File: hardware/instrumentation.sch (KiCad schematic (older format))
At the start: 27 parts, among them U2 TMP235, U3 TMP235, U4 TMP235, U5 TMUX1309, U6 TMUX1309, U7 LMV554

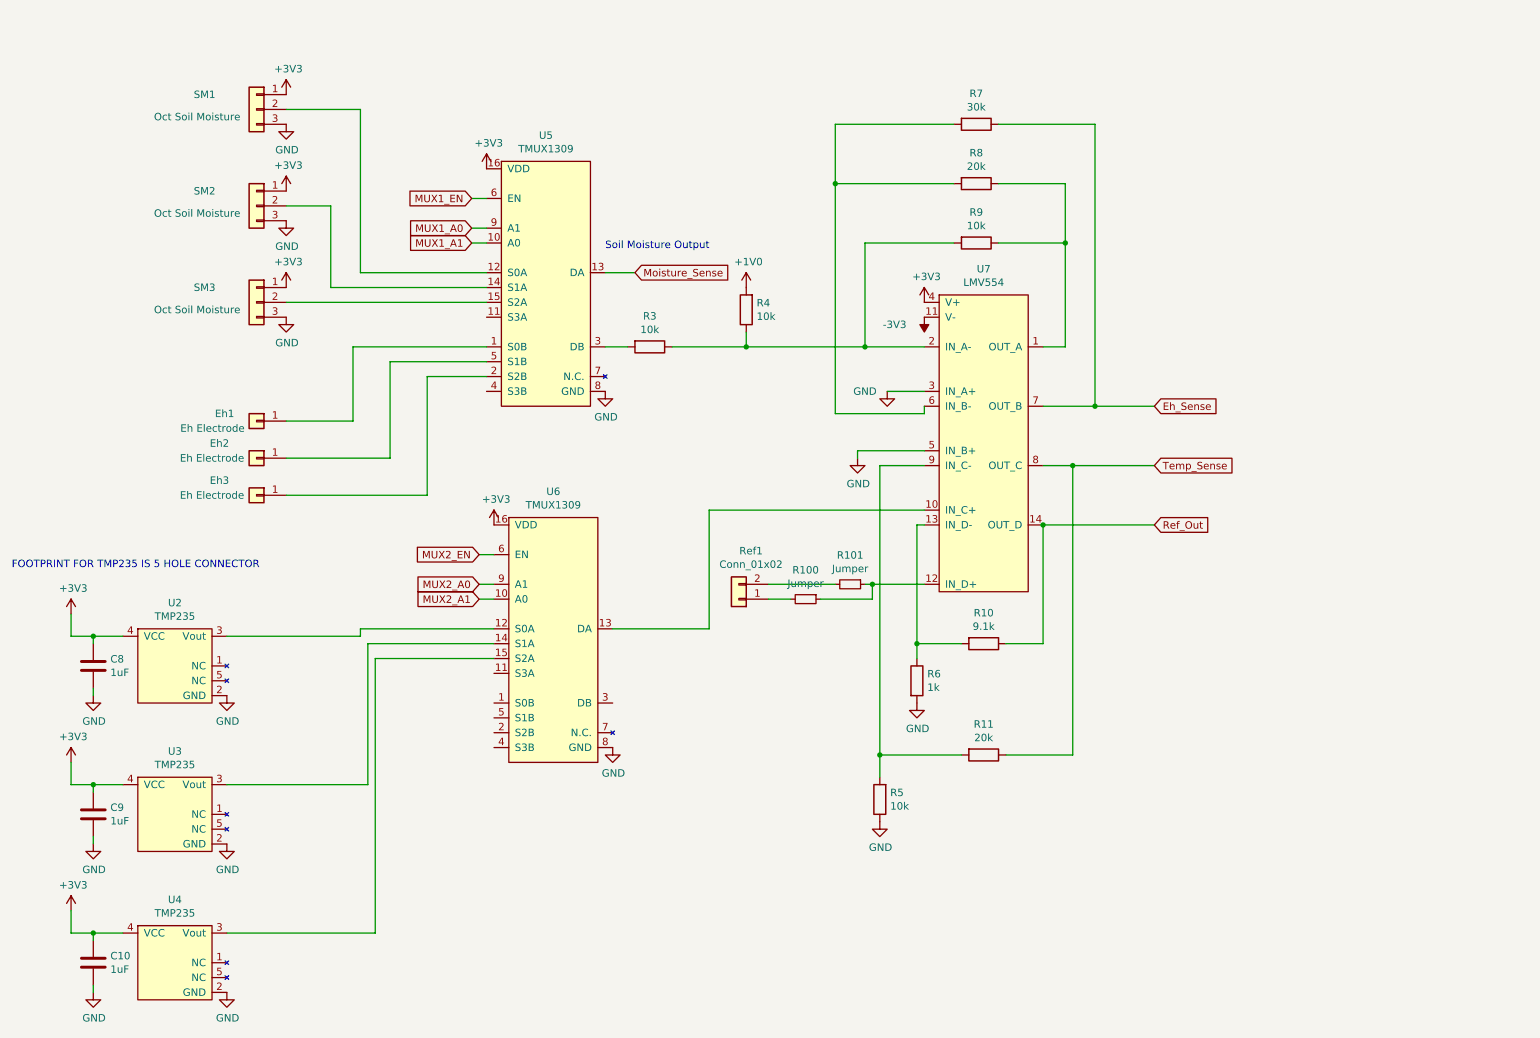
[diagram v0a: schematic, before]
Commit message: Added LMP7721
Added LMP7721 in parallel to op amp A channel circuit. Added jumpers to be able to select path. Added R11 and R12, R8 changed to DNI
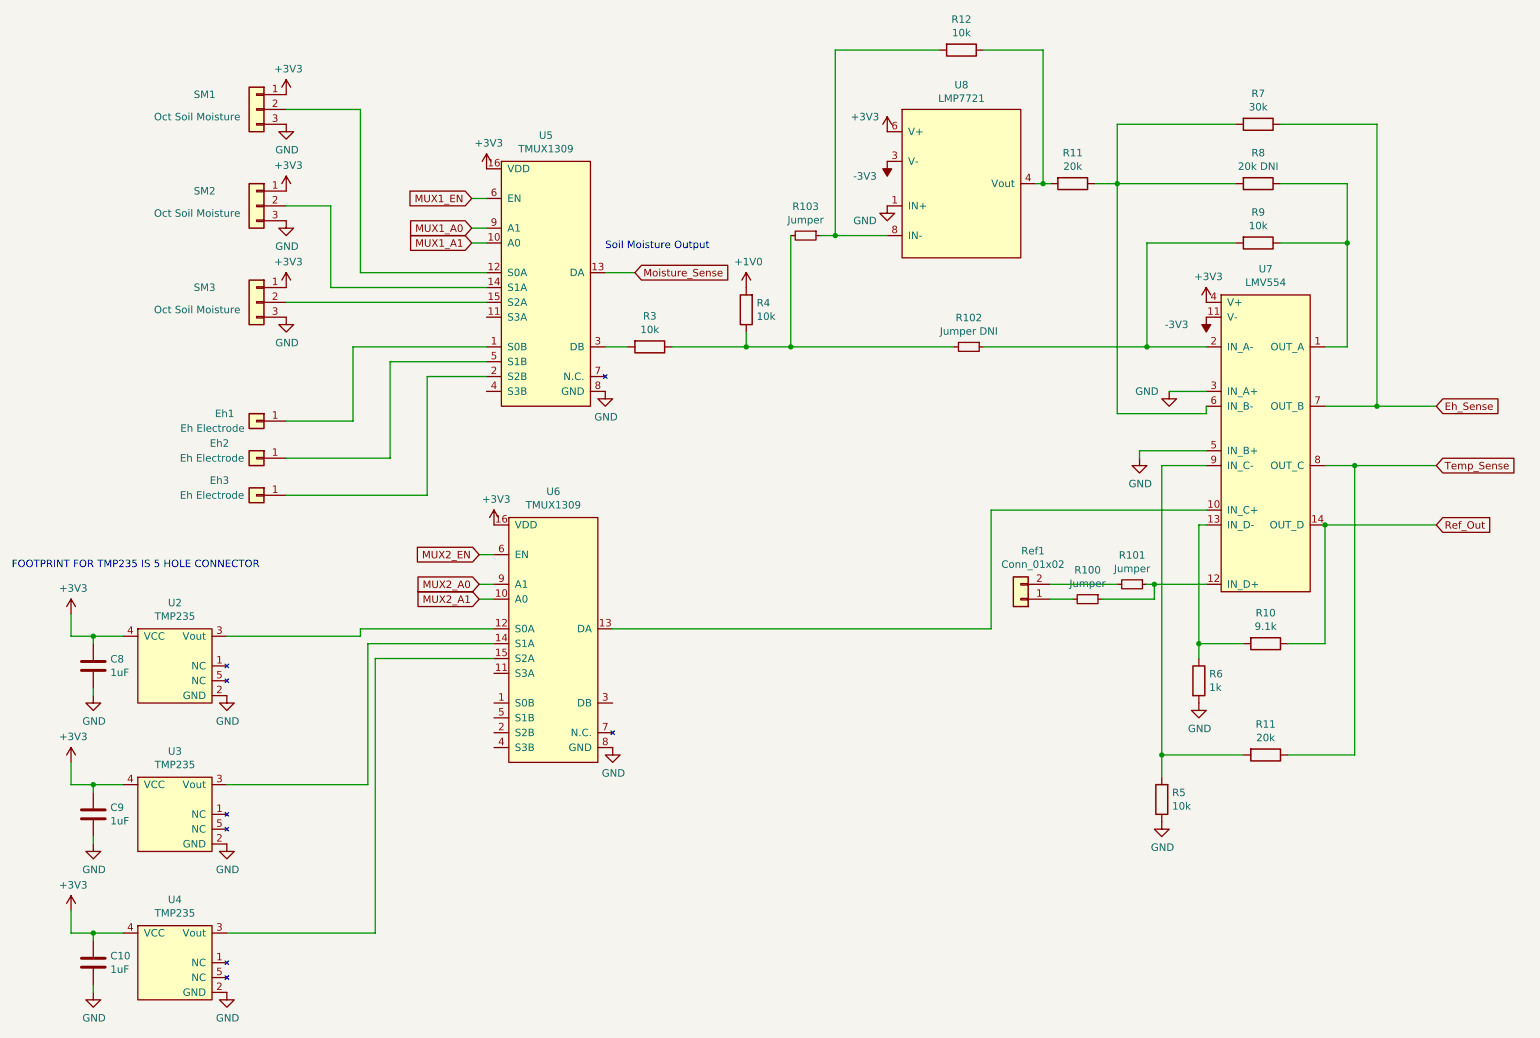
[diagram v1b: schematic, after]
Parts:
- added R102: Jumper DNI, Resistor_SMD:R_0603_1608Metric_Pad0.98x0.95mm_HandSolder, symbol mallard-rescue:R_Small-Device
- added R103: Jumper, Resistor_SMD:R_0603_1608Metric_Pad0.98x0.95mm_HandSolder, symbol mallard-rescue:R_Small-Device
- added R11: 20k, Resistor_SMD:R_0201_0603Metric_Pad0.64x0.40mm_HandSolder, symbol mallard-rescue:R-Device
- added R12: 10k, Resistor_SMD:R_0201_0603Metric_Pad0.64x0.40mm_HandSolder, symbol mallard-rescue:R-Device
- added U8: LMP7721, symbol mallard:LMP7721
- R8: value 20k -> 20k DNI
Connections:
- net +3V3: now also U8.6 (V+)
- net -3V3: now also U8.3 (V-)
- net GND: now also U8.1 (IN+)
- net at R3.1, R4.1: now also R102.2, R103.2; no longer R9.2, U7.2 (IN_A-)
- net at R7.2, R8.2, U7.6 (IN_B-): now also R11.1
- new net: R102.1, R9.2, U7.2 (IN_A-)
- new net: R11.2, R12.1, U8.4 (Vout)
- new net: R103.1, R12.2, U8.8 (IN-)
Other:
- moved on the sheet: R10, R100, R101, R11, R5, R6, R7, R8, R9, Ref1, U7

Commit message: Updated footprint and added decoupling caps
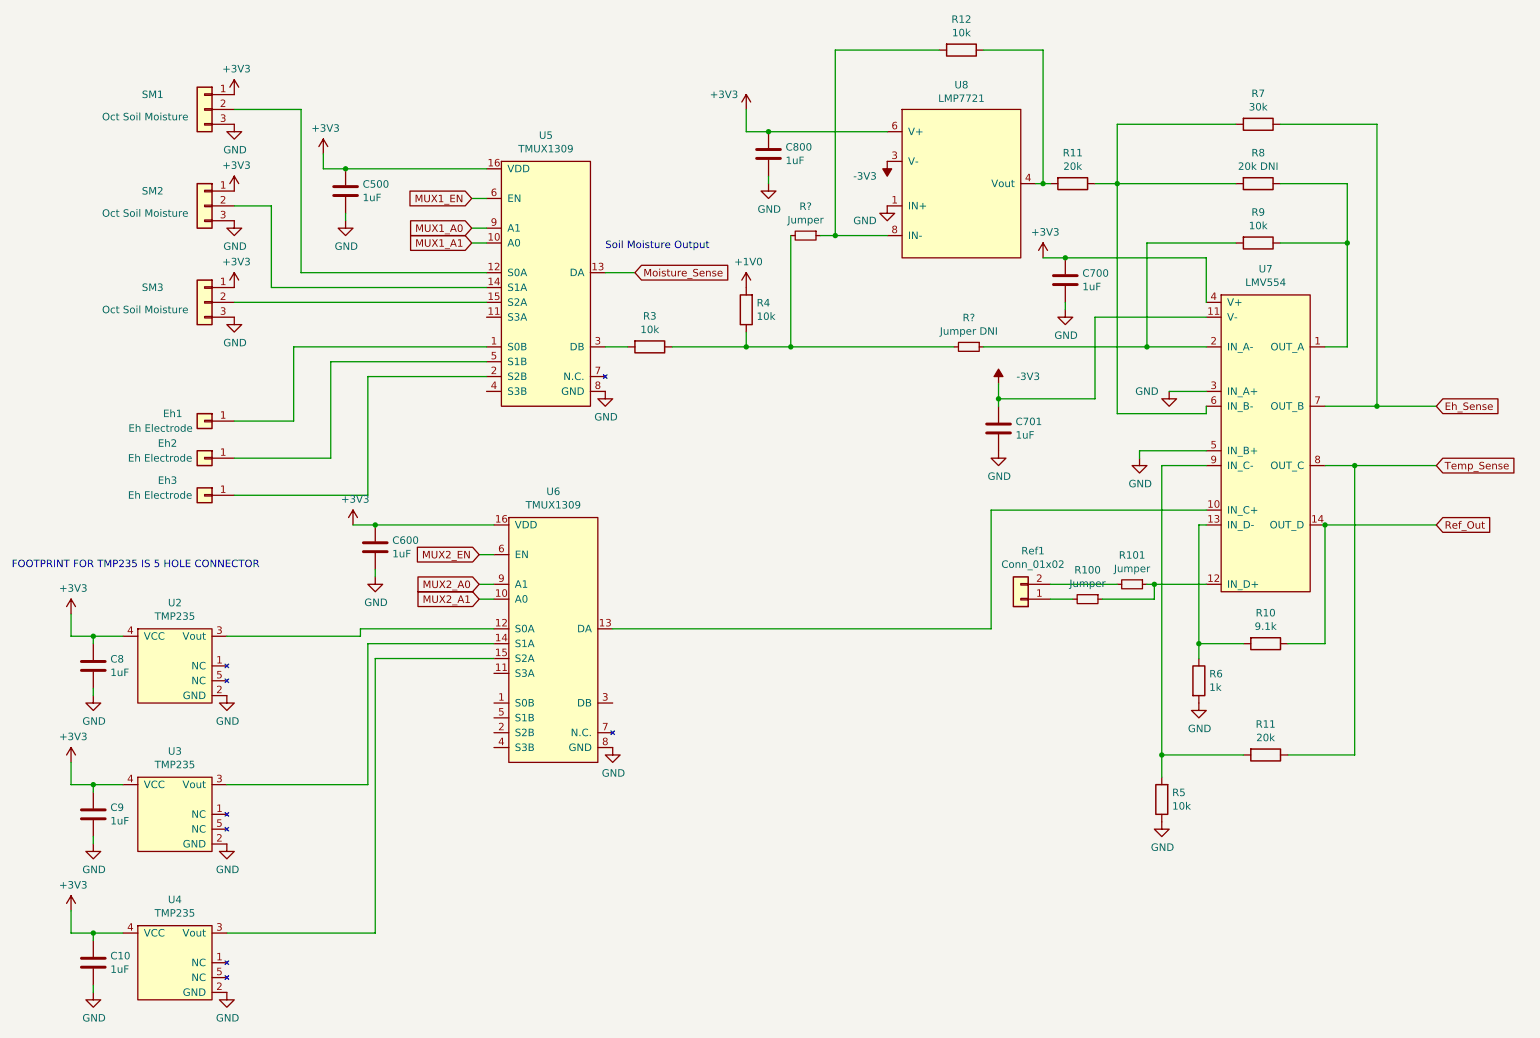
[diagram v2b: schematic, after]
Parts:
- added C500, C600, C700, C701, C800: 1uF, Capacitor_SMD:C_0603_1608Metric_Pad1.08x0.95mm_HandSolder, symbol mallard-rescue:C-Device
- U8: footprint (none) -> Package_SO:SOIC-8_3.9x4.9mm_P1.27mm; Digikey (none) -> LMP7721MA/NOPB-ND
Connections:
- net +3V3: now also C500.1, C600.1, C700.1, C800.1
- net -3V3: now also C701.1
- net GND: now also C500.2, C600.2, C700.2, C701.2, C800.2
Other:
- moved on the sheet: Eh1, Eh2, Eh3, SM1, SM2, SM3
